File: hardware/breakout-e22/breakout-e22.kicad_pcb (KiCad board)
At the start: 2 copper layers, 40.6 x 46.3 mm, 5 parts, among them J1 Conn_01x11, J2 Conn_01x11, U1 E22-170M30S-SX1262

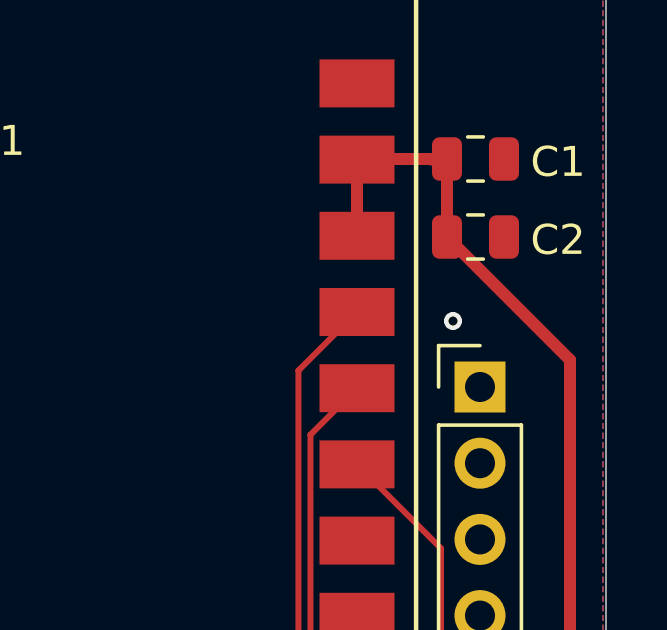
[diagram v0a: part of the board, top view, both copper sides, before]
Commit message: Refonte from scratch carte mère adaptée au breakout E22 + finitions
Carte mère reconçue pour recevoir le breakout E22 plutôt que le module
soudé direct. Trois composants seulement : XIAO ESP32-S3 DIP, plus
deux embases femelles 1×11 (PinSocket_2.54mm) espacées de 32,1 mm
centre à centre pour matcher les pin headers du breakout.

Schéma : labels signaux (NRST, DIO1, BUSY, TXEN, RXEN, NSS, SCK, MISO,
MOSI), power ports +5V (au lieu de +3V3) sur la pin VBUS du XIAO et
les broches VCC du connecteur — alimentation passe maintenant par
VBUS pour permettre la pleine puissance 30 dBm hardware. NC flags sur
DIO2, ANT, et pins XIAO réserve.

PCB compact 80 × 55 mm avec contour Edge.Cuts, USB-C du XIAO en bord
gauche pour découpe boîtier simple. Routage manuel en F.Cu pour
préserver la continuité du plan de masse face arrière, avec inversions
MISO↔MOSI et NRST↔DIO1 dans le firmware pour éliminer les croisements
géométriques. Zones GND coulées sur F.Cu et B.Cu en mode pleine
connexion.

DRC : 0 erreur, 0 pad non connecté. Les warnings restants sont
purement cosmétiques (silkscreen XIAO qui dépasse du bord PCB côté
USB-C — attendu).

Breakout E22 : ajustements mineurs après finalisation du DRC.

.gitignore élargi : **/fab/ pour ignorer les Gerbers de tous les
sous-projets, *-gerbers.zip pour les ZIP d'upload, *.dsn / *.ses pour
les intermédiaires Freerouting.

Co-Authored-By: Claude Opus 4.7 (1M context) <noreply@anthropic.com>
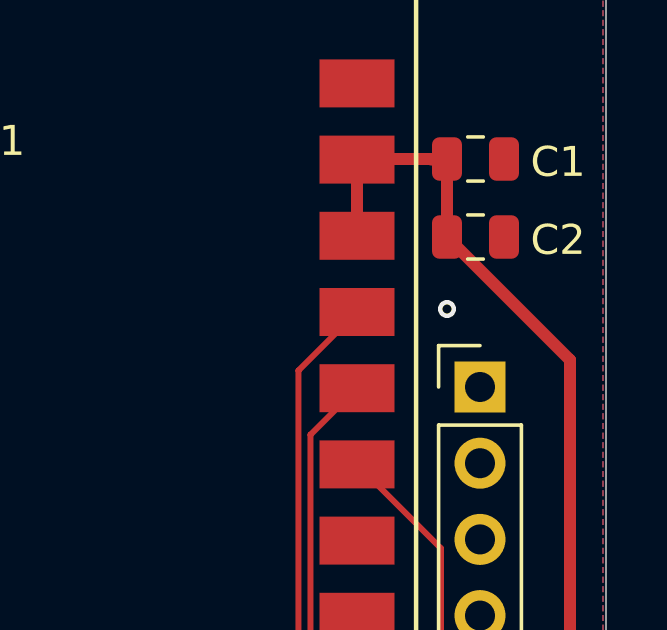
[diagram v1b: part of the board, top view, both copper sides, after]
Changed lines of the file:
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@@
 			(outputformat 1)
 			(mirror no)
-			(drillshape 1)
+			(drillshape 0)
 			(scaleselection 1)
-			(outputdirectory "")
+			(outputdirectory "fab/")
 		)
 	)
@@
 	)
 	(via
-		(at 165.8 91.8)
+		(at 165.6 91.4)
 		(size 0.6)
 		(drill 0.3)
